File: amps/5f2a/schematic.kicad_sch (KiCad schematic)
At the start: 31 parts, among them T2 SE 5k:8

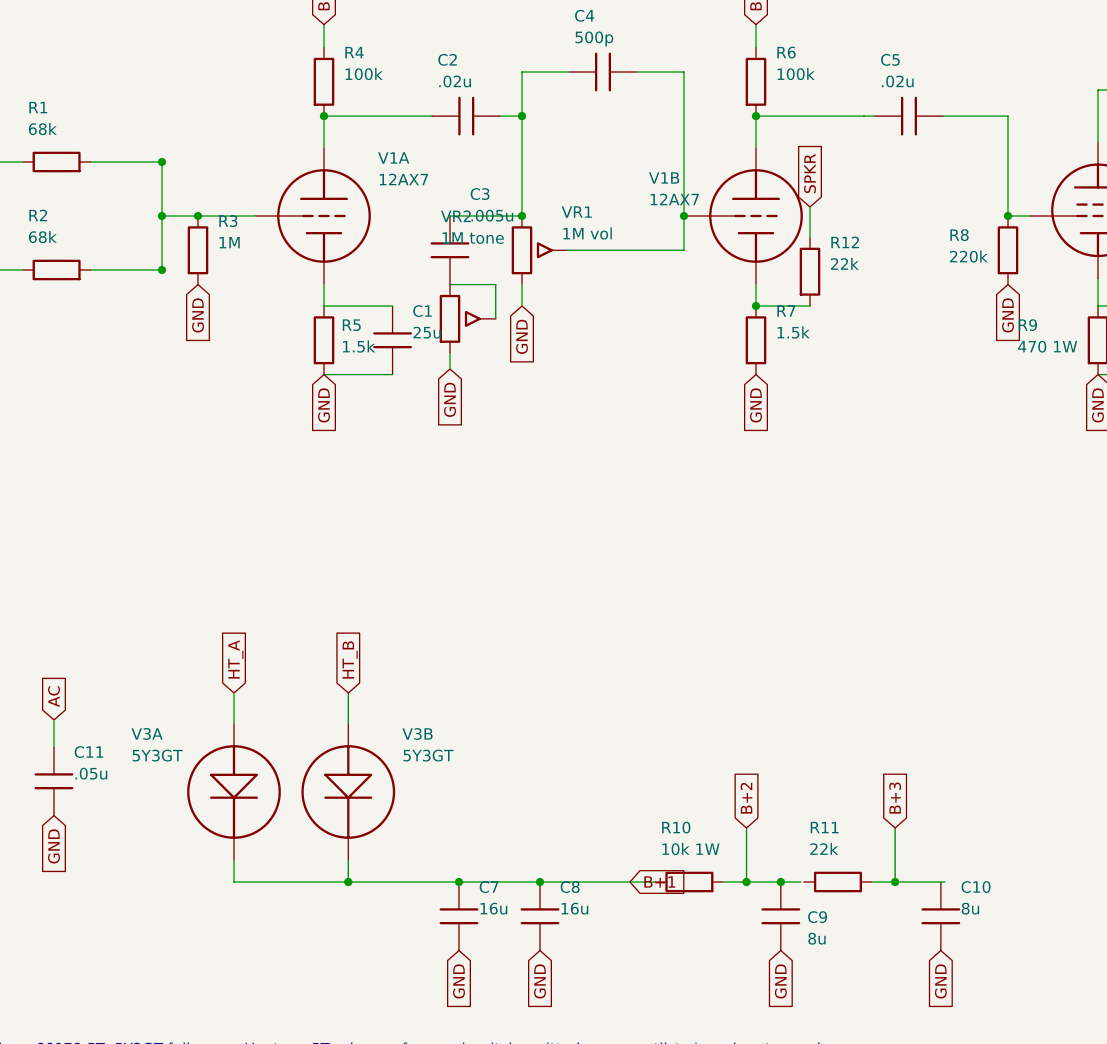
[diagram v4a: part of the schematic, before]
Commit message: Fix: deterministic schematic ids and wires split at every join
- _u() is uuid5 over (amp id, emission order), so a regeneration of an
  unchanged script is byte-identical and a drift gate becomes possible
- write() splits wire segments at symbol pins, wire ends and junction dots,
  so the file connects exactly what the drawing shows under KiCad's
  endpoint-only semantics (270 pins were on a wire's interior; net
  partitions unchanged on all 38 sheets)
- all sheets regenerated; aa864-bassman title block was stale (draft) and
  now matches meta.yaml (verified)

Co-Authored-By: Claude Fable 5.1 <noreply@anthropic.com>
Claude-Session: https://claude.ai/code/session_01KBMfdh37HmCL2iWcBiL5J1
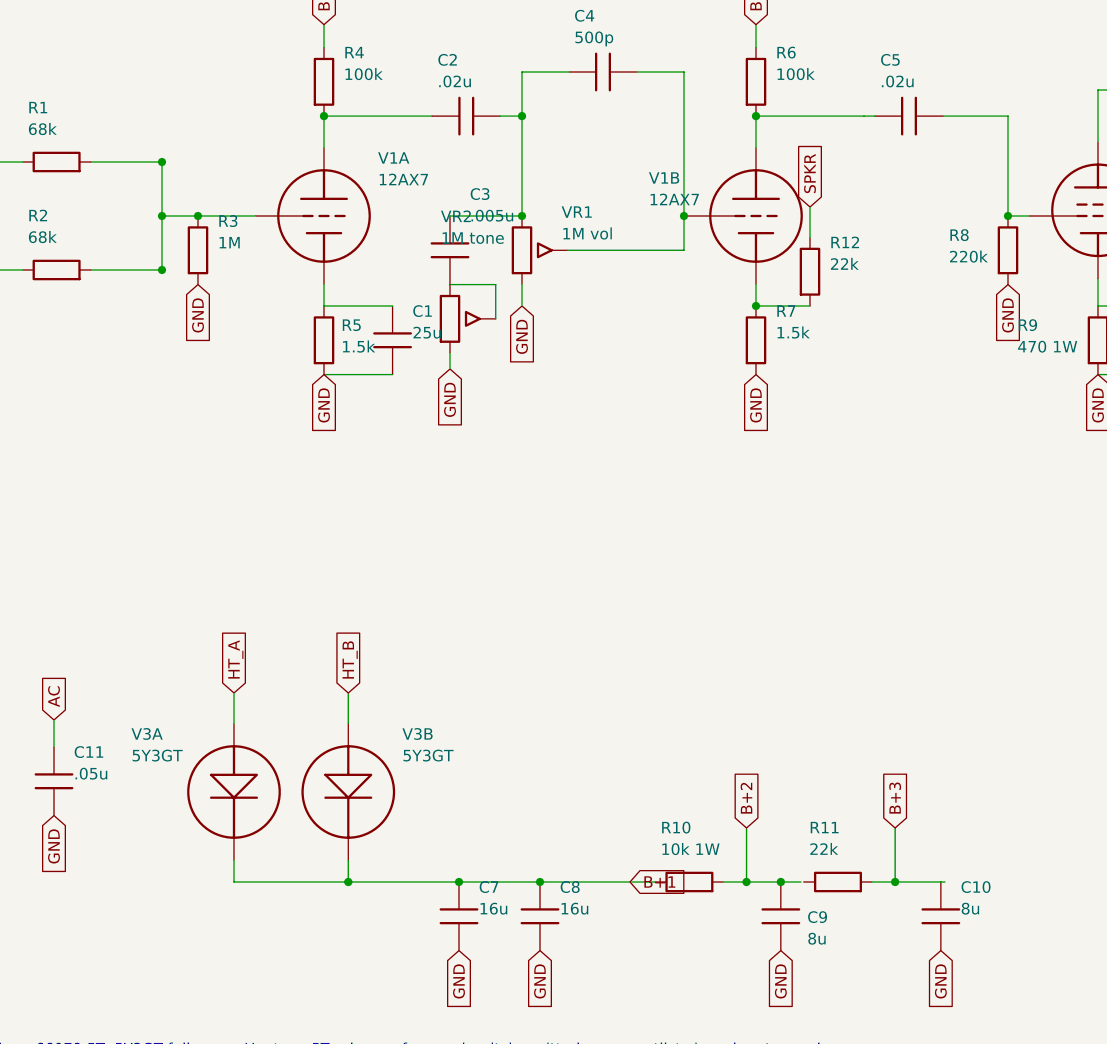
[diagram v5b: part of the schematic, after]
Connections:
- net B+3: now also C10.1
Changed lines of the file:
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@@
   (wire (pts (xy 32.5724 44.278) (xy 40.4724 44.278))
     (stroke (width 0) (type default)))
-  (wire (pts (xy 40.4724 32.278) (xy 40.4724 44.278))
+  (wire (pts (xy 40.4724 32.278) (xy 40.4724 38.278))
+    (stroke (width 0) (type default)))
+  (wire (pts (xy 40.4724 38.278) (xy 40.4724 44.278))
     (stroke (width 0) (type default)))
   (junction (at 40.4724 32.278) (diameter 0) (color 0 0 0 0))
@@
   (wire (pts (xy 61.1724 109.898) (xy 61.1724 112.278))
     (stroke (width 0) (type default)))
-  (wire (pts (xy 48.4724 112.278) (xy 92.4724 112.278))
+  (wire (pts (xy 48.4724 112.278) (xy 61.1724 112.278))
+    (stroke (width 0) (type default)))
+  (wire (pts (xy 61.1724 112.278) (xy 73.4724 112.278))
+    (stroke (width 0) (type default)))
+  (wire (pts (xy 73.4724 112.278) (xy 82.4724 112.278))
+    (stroke (width 0) (type default)))
+  (wire (pts (xy 82.4724 112.278) (xy 92.4724 112.278))
     (stroke (width 0) (type default)))
   (junction (at 61.1724 112.278) (diameter 0) (color 0 0 0 0))
@@
     (property "Reference" "R10" (at 95.8724 106.278 270) (effects (font (size 1.27 1.27)) (justify left)))
     (property "Value" "10k 1W" (at 95.8724 108.678 270) (effects (font (size 1.27 1.27)) (justify left))))
-  (wire (pts (xy 102.882 112.278) (xy 111.472 112.278))
+  (wire (pts (xy 102.882 112.278) (xy 105.422 112.278))
+    (stroke (width 0) (type default)))
+  (wire (pts (xy 105.422 112.278) (xy 109.232 112.278))
+    (stroke (width 0) (type default)))
+  (wire (pts (xy 109.232 112.278) (xy 111.472 112.278))
     (stroke (width 0) (type default)))
   (junction (at 105.422 112.278) (diameter 0) (color 0 0 0 0))
@@
     (property "Reference" "R11" (at 112.382 106.278 270) (effects (font (size 1.27 1.27)) (justify left)))
     (property "Value" "22k" (at 112.382 108.678 270) (effects (font (size 1.27 1.27)) (justify left))))
-  (wire (pts (xy 119.392 112.278) (xy 127.472 112.278))
+  (wire (pts (xy 119.392 112.278) (xy 121.932 112.278))
+    (stroke (width 0) (type default)))
+  (wire (pts (xy 121.932 112.278) (xy 127.012 112.278))
+    (stroke (width 0) (type default)))
+  (wire (pts (xy 127.012 112.278) (xy 127.472 112.278))
     (stroke (width 0) (type default)))
   (junction (at 121.932 112.278) (diameter 0) (color 0 0 0 0))

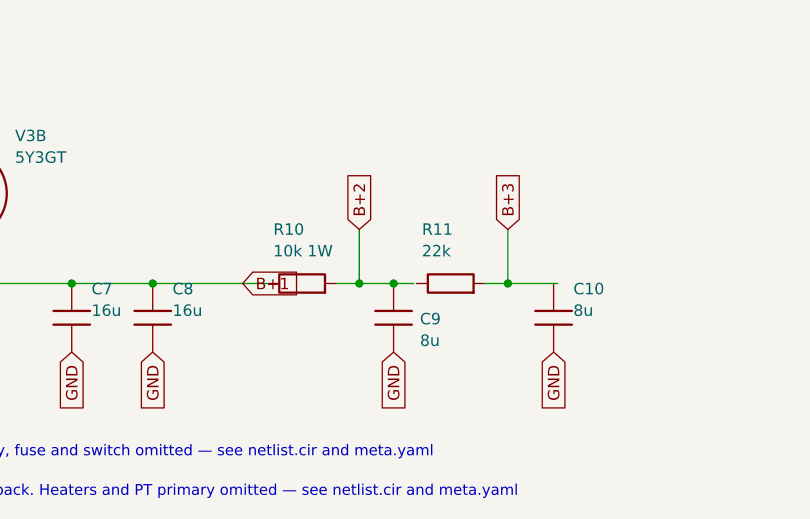
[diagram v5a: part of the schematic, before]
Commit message: Fix: schematic wiring on the tweed family, jtm45 and 6161
- pot cold lugs: s.gnd() sat 3.81 mm below cx:POT pin 3 on nine sheets
  (19 pins); every flag now lands on the lug
- retyped coordinates replaced by helper returns (5e5a OT pins alone freed
  nine pins; 5d3 V3 cathode, 5f10 RKB, 5e6a CBS, 5f2a dropper, grid leaks)
- shorts only verify_schematic_nets could see: 5e3 cathode bus through V4's
  screen pin (B+2 tied to the cathodes), C7 through RG6A, PI leak through
  RGPI, C8 on the cathode not the tail; 5f10 the same RGPI/C7 pair; 5e5a
  presence feed down the tube column; 5e6a RFB loop through RL3
- three dated waivers: two-terminal rheostat far lugs (5e6a VR5, 6161 VR3/VR4)

Co-Authored-By: Claude Fable 5.1 <noreply@anthropic.com>
Claude-Session: https://claude.ai/code/session_01KBMfdh37HmCL2iWcBiL5J1
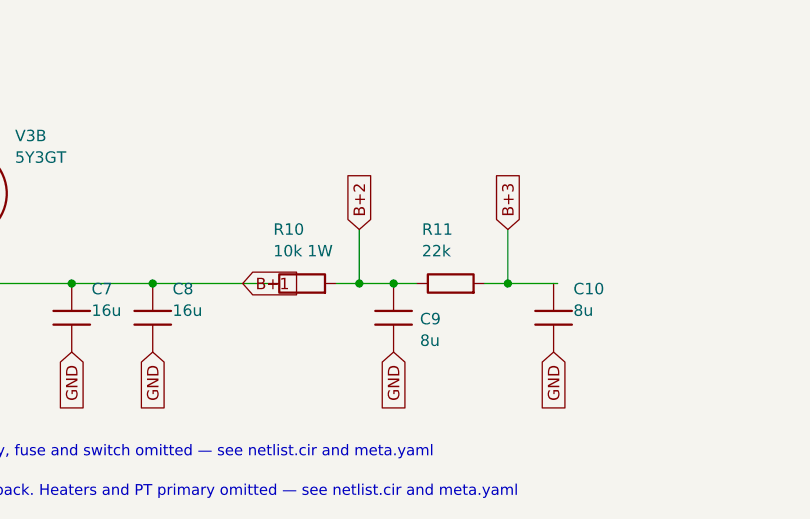
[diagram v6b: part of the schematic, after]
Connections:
- net B+2: now also R11.1
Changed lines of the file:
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@@
     (property "Reference" "R10" (at 95.8724 106.278 270) (effects (font (size 1.27 1.27)) (justify left)))
     (property "Value" "10k 1W" (at 95.8724 108.678 270) (effects (font (size 1.27 1.27)) (justify left))))
-  (wire (pts (xy 102.882 112.278) (xy 105.422 112.278))
-    (stroke (width 0) (type default)))
-  (wire (pts (xy 105.422 112.278) (xy 109.232 112.278))
-    (stroke (width 0) (type default)))
-  (wire (pts (xy 109.232 112.278) (xy 111.472 112.278))
-    (stroke (width 0) (type default)))
   (junction (at 105.422 112.278) (diameter 0) (color 0 0 0 0))
   (global_label "B+2" (shape input) (at 105.422 106.278 90)
@@
     (property "Reference" "R11" (at 112.382 106.278 270) (effects (font (size 1.27 1.27)) (justify left)))
     (property "Value" "22k" (at 112.382 108.678 270) (effects (font (size 1.27 1.27)) (justify left))))
+  (wire (pts (xy 102.882 112.278) (xy 105.422 112.278))
+    (stroke (width 0) (type default)))
+  (wire (pts (xy 105.422 112.278) (xy 109.232 112.278))
+    (stroke (width 0) (type default)))
+  (wire (pts (xy 109.232 112.278) (xy 111.772 112.278))
+    (stroke (width 0) (type default)))
   (wire (pts (xy 119.392 112.278) (xy 121.932 112.278))
     (stroke (width 0) (type default)))
